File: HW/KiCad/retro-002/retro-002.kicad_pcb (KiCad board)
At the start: 2 copper layers, 100 x 100 mm, 352 parts, among them J1 Conn_02x05_JTAG, J100 x, J101 x, J102 x, J103 x, J104 x, J105 x, J106 x, J12 Reset, J2 Conn_02x05_JTAG, J21 x, J22 x, J3 Serial, J37 x, J38 x, J39 x, J4 SysBus, J40 x, J41 x, J42 x, J43 x, J44 x, J45 x, J46 x, J47 x, J48 x, J49 x, J50 x, J51 x, J52 x, J53 x, J54 x, J55 x, J56 x, J57 x, J58 x, J59 x, J6 SysBus, J60 x, J61 x, J62 x, J63 x, J64 x, J65 x, J66 x, J67 x, J68 x, J69 x, J7 Conn_01x16_Pin, J70 x, J71 x, J72 x, J73 x, J74 x, J75 x, J76 x, J77 x, J78 x, J79 x, J80 x, J81 x, J82 x, J83 x, J84 x, J85 x, J86 x, J87 x, J88 x, J89 x, J90 x, J91 x, J92 x, J93 x, J94 x, J95 x, J96 x, J97 x, J98 x, J99 x, M3 CY7C109D-10ZXI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

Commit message: nejaka zmena
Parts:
- moved R63 3.42 mm to (186.3, 44.5)
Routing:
- net +5V: track 778.6 -> 641.0 mm, vias 9 -> 20
- net GND: track 830.2 -> 768.0 mm, vias 9 -> 17
- net ~{Dev_Sel_0}: track 149.0 -> 94.4 mm, vias 3 -> 6
- net /mA_SHARE_DIRTY: track 131.9 -> 87.5 mm, vias 3 -> 2
- net D4: track 233.2 -> 192.9 mm, vias 4 -> 8
- net ~{Read}: track 150.5 -> 111.4 mm, vias 1 -> 2
- net /mB_SHARE_DIRTY: track 126.7 -> 88.2 mm
- net B_G_ENABLE: track 100.9 -> 67.8 mm, vias 1 -> 3
- net A_G_A_DIR: track 96.2 -> 64.5 mm, vias 2 -> 1
- net /~{Dev_2}: track 104.3 -> 132.7 mm, vias 2 -> 3
- net A_G_ENABLE: track 90.9 -> 63.4 mm, vias 3 -> 2
- net MR3: track 95.9 -> 68.5 mm
- net D7: track 203.8 -> 176.5 mm, vias 5 -> 6
- net D2: track 206.7 -> 180.3 mm, vias 3 -> 6
- net D1: track 209.8 -> 186.0 mm, vias 7 -> 5
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
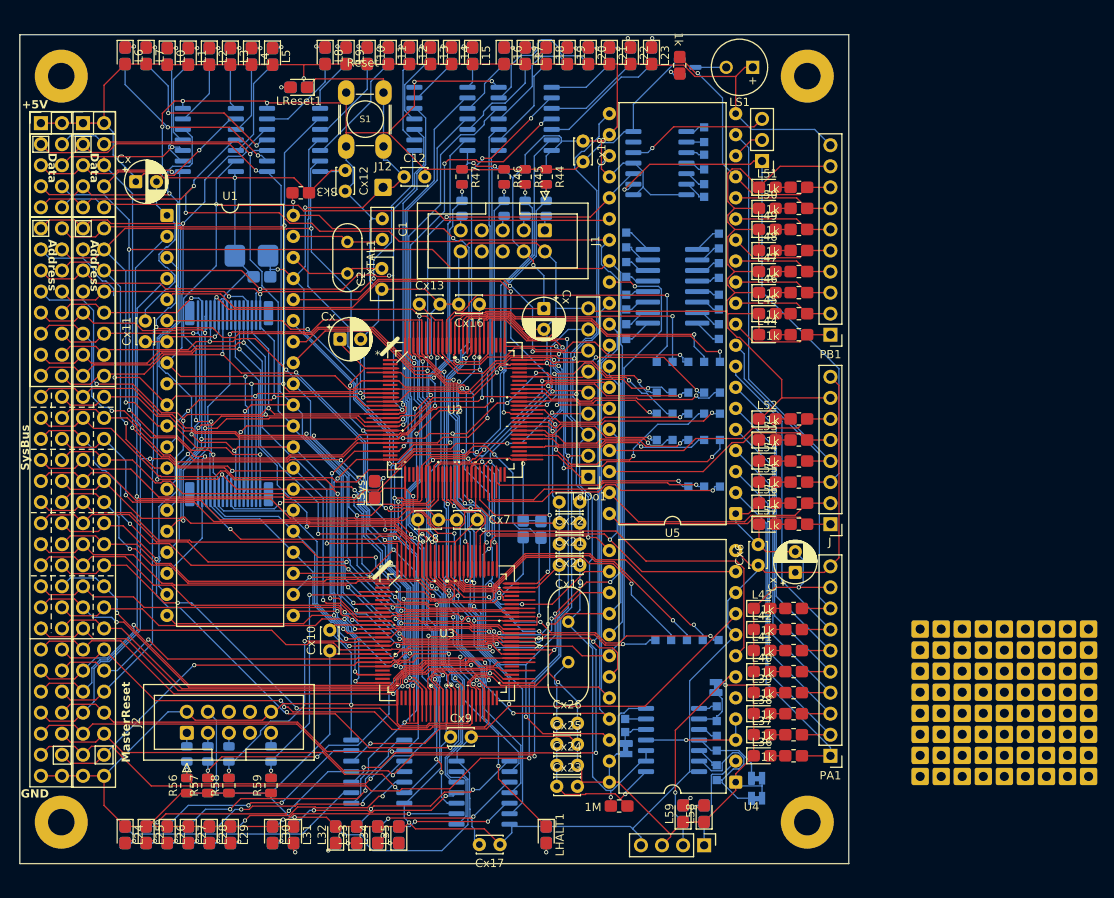
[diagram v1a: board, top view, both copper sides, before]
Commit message: Pridana EEPROM, ucesano, pridana rozpracovana PLD
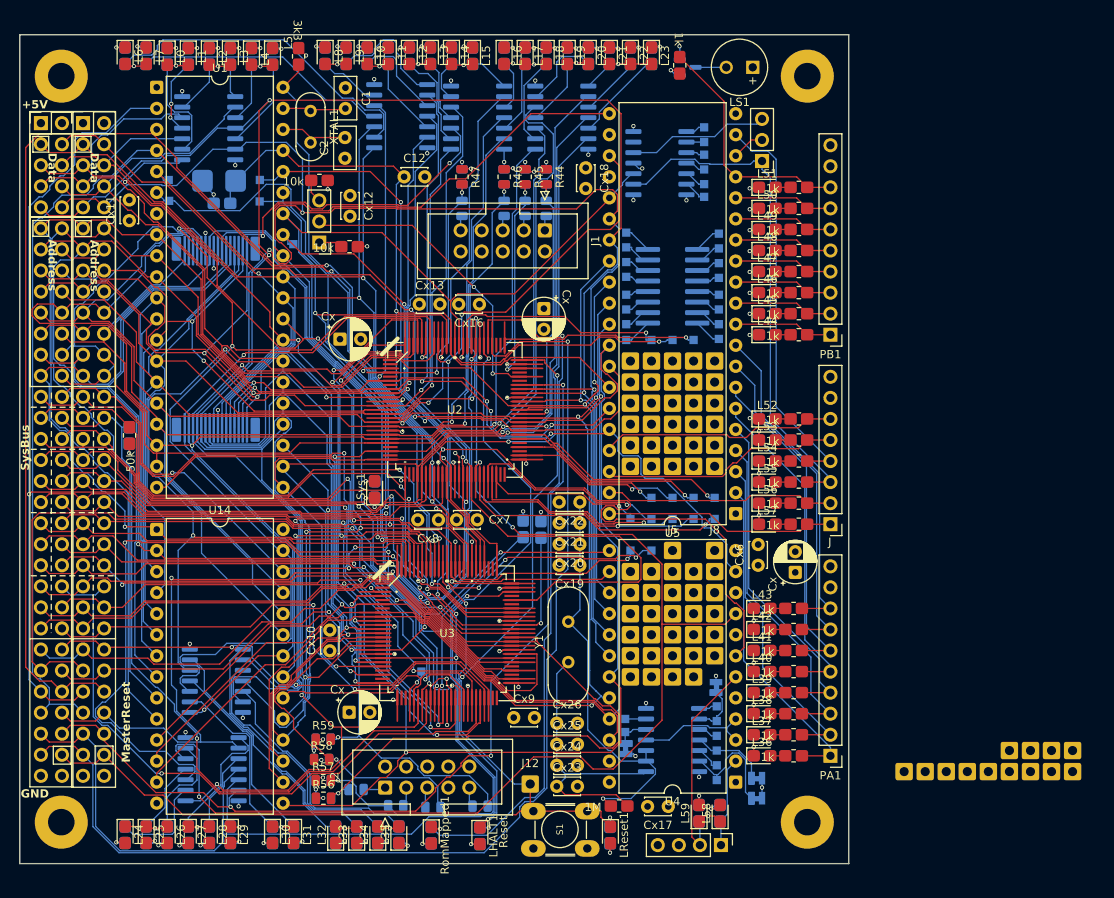
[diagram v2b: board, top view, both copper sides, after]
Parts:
- removed TP38, TP39, TP40, TP41, TP42, TP43, TP44, TP45, TP46, TP47, TP48: IO, MHF:TestPoint_Pad_1.0x1.0mm
- removed TP66, TP68, TP69, TP71, TP73, TP74: I, MHF:TestPoint_Pad_1.0x1.0mm
- removed ToDo1: J, MHF:PinHeader_1x09_P2.54mm_Vertical
- added J5: x, MHF:PinHole_1x01_2.54xrectangle, F.Cu at (231.1, 87.6)
- added J8: x, MHF:PinHole_1x01_2.54xrectangle, F.Cu at (236.2, 87.6)
- added Jx2: BootFrom, MHF:PinHeader_1x03_P2.54mm_Vertical, F.Cu at (188.5, 50.5)
- added R93: 50k, MHF:R_0805_2012Metric_Pad1.20x1.40mm_HandSolder, F.Cu at (165.6, 73.7)
- added R94: 50k, MHF:R_0805_2012Metric_Pad1.20x1.40mm_HandSolder, B.Cu at (165.6, 73.8)
- added R95: 10k, MHF:R_0805_2012Metric_Pad1.20x1.40mm_HandSolder, F.Cu at (192.2, 51.0)
- added R96: 10k, MHF:R_0805_2012Metric_Pad1.20x1.40mm_HandSolder, F.Cu at (188.5, 43.0)
- added R97: 1k, MHF:R_0805_2012Metric_Pad1.20x1.40mm_HandSolder, B.Cu at (202.0, 122.0)
- added RomMapped1: RomMapped, MHF:LED_0805_2012Metric, F.Cu at (202.0, 122.0)
- added TP31: DEV7, MHF:TestPoint_Pad_1.0x1.0mm, B.Cu at (233.7, 62.2)
- added TP32: DMA, MHF:TestPoint_Pad_1.0x1.0mm, B.Cu at (185.4, 50.7)
- added TP33: MRDY, MHF:TestPoint_Pad_1.0x1.0mm, B.Cu at (181.4, 42.9)
- added TP34: BA, MHF:TestPoint_Pad_1.0x1.0mm, B.Cu at (170.4, 45.4)
- added TP35: BS, MHF:TestPoint_Pad_1.0x1.0mm, B.Cu at (170.4, 42.9)
- added TP36: Q, MHF:TestPoint_Pad_1.0x1.0mm, B.Cu at (181.3, 45.5)
- added TP56: IO, MHF:TestPoint_Pad_1.0x1.0mm, B.Cu at (231.1, 83.8)
- added TP57: IO, MHF:TestPoint_Pad_1.0x1.0mm, B.Cu at (226.1, 83.8)
- added TP58: IO, MHF:TestPoint_Pad_1.0x1.0mm, B.Cu at (200.8, 102.2)
- added U14: 28C256, Package_DIP:DIP-28_W15.24mm, F.Cu at (168.9, 85.1)
- U4: footprint Package_DIP:DIP-24_W15.24mm -> Gilhad_footprints:DIP-24_W15.24mm
- U5: footprint Package_DIP:DIP-40_W15.24mm -> Gilhad_footprints:DIP-40_W15.24mm
- moved R66 97.7 mm to (223.6, 122.0), turned to 90 degrees
- moved LReset1 97.7 mm to (223.6, 121.9), turned to -90 degrees
- moved S1 93.9 mm to (214.4, 123.6), turned to 90 degrees
- moved J12 74.1 mm to (214.0, 115.8)
- moved Cx27 69.0 mm to (192.1, 107.1)
- moved J78 48.2 mm to (228.6, 97.8)
- moved J79 48.2 mm to (228.6, 100.3)
- moved J80 48.2 mm to (228.6, 102.9)
- moved J84 48.2 mm to (228.6, 92.7)
- moved J85 48.2 mm to (228.6, 95.2)
- moved J92 48.2 mm to (228.6, 90.2)
- moved J100 48.2 mm to (233.7, 92.7)
- moved J101 48.2 mm to (233.7, 95.2)
- moved J102 48.2 mm to (233.7, 97.8)
- moved J103 48.2 mm to (233.7, 100.3)
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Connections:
- net /mA_HALT renamed /A_HALT
- net /mA_READ renamed /A_READ
- net /mA_SHARE_DIRTY renamed /A_SHARE_DIRTY
- net /mA_SHARE_GRANTED renamed /A_SHARE_GRANTED
- net /mA_SHARE_REQUEST renamed /A_SHARE_REQUEST
- net /mA_SHARE_SELECT renamed /A_SHARE_SELECT
- net /mA_S_16 renamed /A_S_16
- net /~{Dev_2} renamed /~{Dev_Sel_4}
- net ~{Dev_Sel_0} renamed ~{RAM}
- TP65 pad 1: Net-(U2-INPUT/OE2/GCLK2) -> Net-(U2-I/O/GCLK3)
- TP70 pad 1: Net-(U3-INPUT/OE2/GCLK2) -> Net-(U3-I/O/GCLK3)
- U2 pad 31: /E -> /R~{W}
- U2 pad 32: /R~{W} -> ~{HALT}
- U2 pad 33: MasterReset -> BA
- U2 pad 35: ~{HALT} -> /~{NMI}
- U2 pad 36: BA -> /~{IRQ}
- U2 pad 37: /~{NMI} -> /~{FIRQ}
- U2 pad 40: /~{IRQ} -> ~{DMA/BREQ}
- U2 pad 41: /~{FIRQ} -> MRDY
- U2 pad 42: ~{DMA/BREQ} -> BS
- U2 pad 44: MRDY -> Net-(TP55-Pad1)
- U2 pad 45: BS -> Net-(TP54-Pad1)
- U2 pad 46: Net-(TP55-Pad1) -> Net-(TP53-Pad1)
- U2 pad 47: Net-(TP54-Pad1) -> Net-(TP56-Pad1)
- U2 pad 48: Net-(TP53-Pad1) -> Net-(TP57-Pad1)
- U2 pad 52: Net-(TP52-Pad1) -> Net-(TP49-Pad1)
- U2 pad 54: Net-(TP51-Pad1) -> Net-(TP50-Pad1)
- U2 pad 56: Net-(TP50-Pad1) -> Net-(TP51-Pad1)
- U2 pad 57: Net-(TP49-Pad1) -> Net-(TP52-Pad1)
- U2 pad 58: Net-(TP48-Pad1) -> D0
- U2 pad 60: Net-(TP47-Pad1) -> D1
- U2 pad 61: Net-(TP46-Pad1) -> D2
- U2 pad 63: Net-(TP45-Pad1) -> D3
- U2 pad 64: Net-(TP44-Pad1) -> D4
- U2 pad 65: Net-(TP43-Pad1) -> D5
- U2 pad 67: Net-(TP42-Pad1) -> D6
- U2 pad 68: Net-(TP41-Pad1) -> D7
- U2 pad 69: Net-(TP40-Pad1) -> /RomMapped
- U2 pad 71: Net-(TP39-Pad1) -> /BootSrc
- U2 pad 75: Net-(TP38-Pad1) -> ~{ROM}
- U2 pad 87: Net-(U2-INPUT/GCLK1) -> /E
- U2 pad 89: Net-(U2-INPUT/GCLR) -> MasterReset
- U2 pad 90: Net-(U2-INPUT/OE2/GCLK2) -> Q
- U3 pad 17: /E -> /R~{W}
- U3 pad 19: /R~{W} -> ~{HALT}
- U3 pad 20: MasterReset -> CA12
- U3 pad 21: ~{HALT} -> CA13
- U3 pad 23: CA12 -> CA14
- U3 pad 25: CA13 -> CA15
- U3 pad 29: CA14 -> Net-(TP58-Pad1)
- U3 pad 30: CA15 -> ~{ROM}
- U3 pad 87: Net-(U3-INPUT/GCLK1) -> /E
- U3 pad 89: Net-(U3-INPUT/GCLR) -> MasterReset
- U3 pad 90: Net-(U3-INPUT/OE2/GCLK2) -> Q
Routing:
- net GND: track 768.0 -> 106.6 mm, vias 17 -> 60
- net +5V: track 641.0 -> 120.6 mm, vias 20 -> 55
- net D6: track 193.6 -> 275.1 mm, vias 5 -> 3
- net ~{ROM}: track 0.00 -> 73.8 mm, vias 0 -> 2
- net /RomMapped: track 0.00 -> 71.2 mm, vias 0 -> 1
- net D1: track 186.0 -> 251.7 mm, vias 5 -> 3
- net D7: track 176.5 -> 241.1 mm, vias 6 -> 4
- net D3: track 175.0 -> 232.5 mm, vias 7 -> 4
- net D0: track 189.5 -> 242.0 mm, vias 7 -> 3
- net /CA2: track 103.5 -> 155.6 mm, vias 3 -> 2
- net /CA1: track 136.6 -> 188.4 mm, vias 5 -> 4
- net /CA0: track 169.7 -> 220.8 mm, vias 5 -> 4
- net /~{IRQ}: track 175.8 -> 226.4 mm, vias 4 -> 2
- net D4: track 192.9 -> 243.2 mm, vias 8 -> 3
- net ~{Dev_Sel_2}: track 102.6 -> 152.3 mm
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- added copper zone on In1.Cu, net +5V
- added copper zone on In2.Cu, net GND
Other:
- copper layers 2 -> 4
